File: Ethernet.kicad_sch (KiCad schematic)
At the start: 1 part

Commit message: Wire Ethernet
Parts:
- added R? (x2): 470Ω, symbol Device:R_Small
- added U? (x2): TPD4EUSB30, Package_SON:USON-10_2.5x1.0mm_P0.5mm, symbol Power_Protection:TPD4EUSB30
- gave numbers to parts that had none: 1
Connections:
- net TD1+: now reaches J.1 (TD1+)
- net TD1+: now also U?.1 (D1+)
- net TD4-: now reaches J.10 (TD4-)
- net TD4-: now also U?.5 (D2-)
- net VC1: now reaches J.11 (VC1)
- net VC2: now reaches J.12 (VC2)
- net VC3: now reaches J.13 (VC3)
- net VC4: now reaches J.14 (VC4)
- net +3.3V: now reaches J.15 (LED1+)
- net +3.3V: now also J.17 (LED2+)
- net at J.16 (LED1-): now also R?.2
- net at J.18 (LED2-): now also R?.2
- net TD1-: now reaches J.2 (TD1-)
- net TD1-: now also U?.2 (D1-)
- net TD2+: now reaches J.3 (TD2+)
- net TD2+: now also U?.4 (D2+)
- net TD2-: now reaches J.6 (TD2-)
- net TD2-: now also U?.5 (D2-)
- net TD3+: now reaches J.7 (TD3+)
- net TD3+: now also U?.1 (D1+)
- net TD3-: now reaches J.8 (TD3-)
- net TD3-: now also U?.2 (D1-)
- net TD4+: now reaches J.9 (TD4+)
- net TD4+: now also U?.4 (D2+)
- net GND: now reaches J.SH
- new net: U?.3 (GND), U?.8 (GND) (x2)
- new net LED_GREEN: R?.1
- new net LED_YELLOW: R?.1
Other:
- moved on the sheet: J

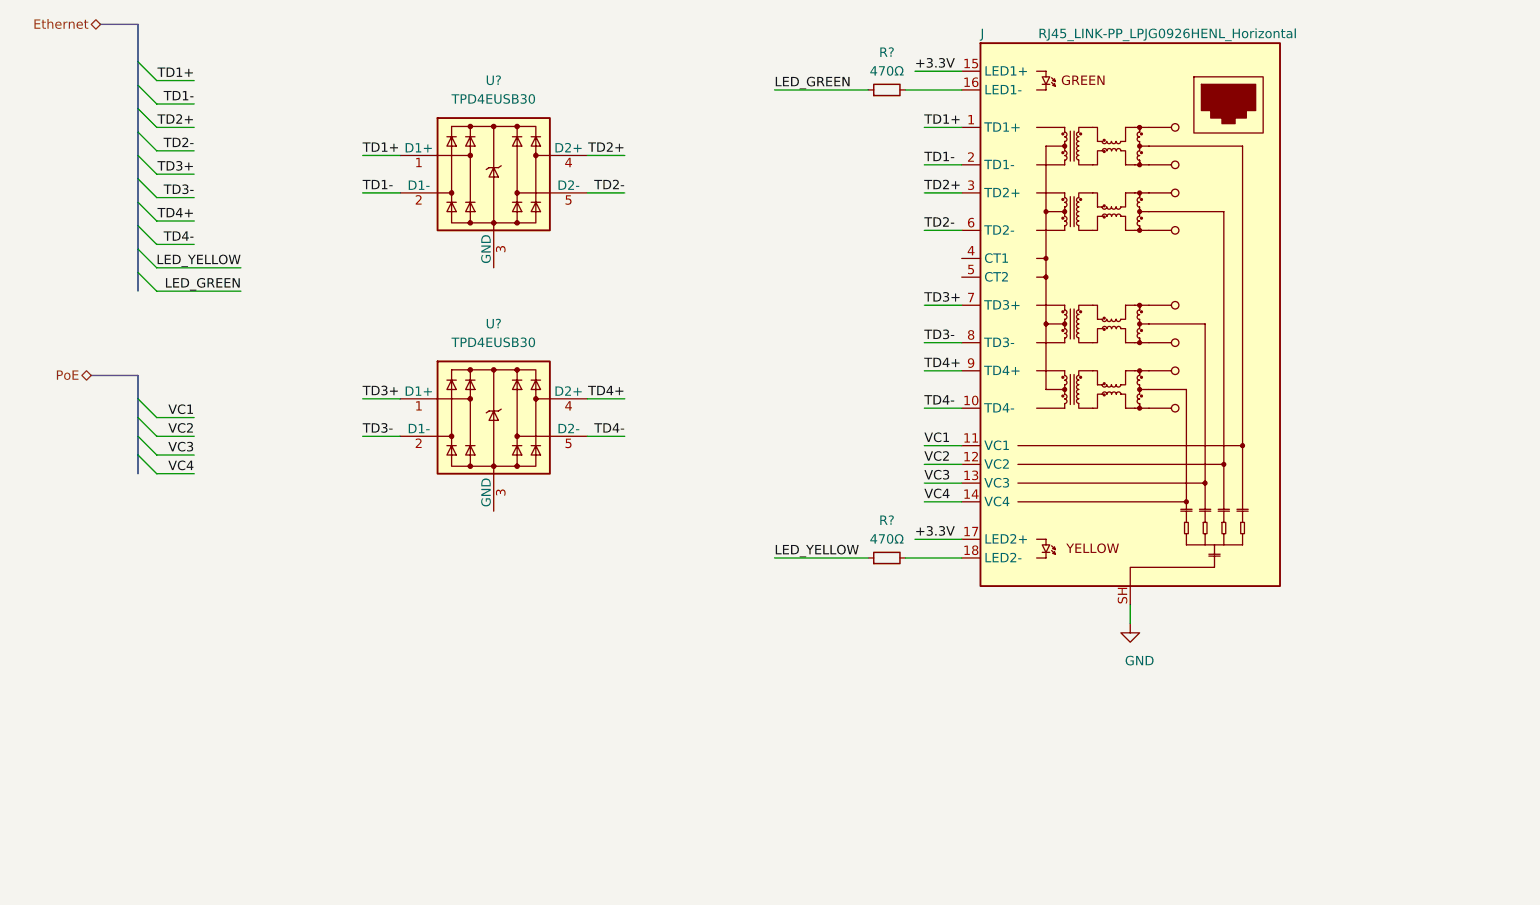
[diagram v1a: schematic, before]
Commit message: Multiple changes in schematic & projects:
    -Added net classes for controlled impedance traces
    -Added power hierarchical sheet
    -Initial USB subsystem schematic
    -Added multiple bus definitions (usb, pcie, i2c etc.)
    -Fixed busses use
    -Added LDO for audio analog rails

Signed-off-by: Dominik Sliwa <dominik@sliwa.io>
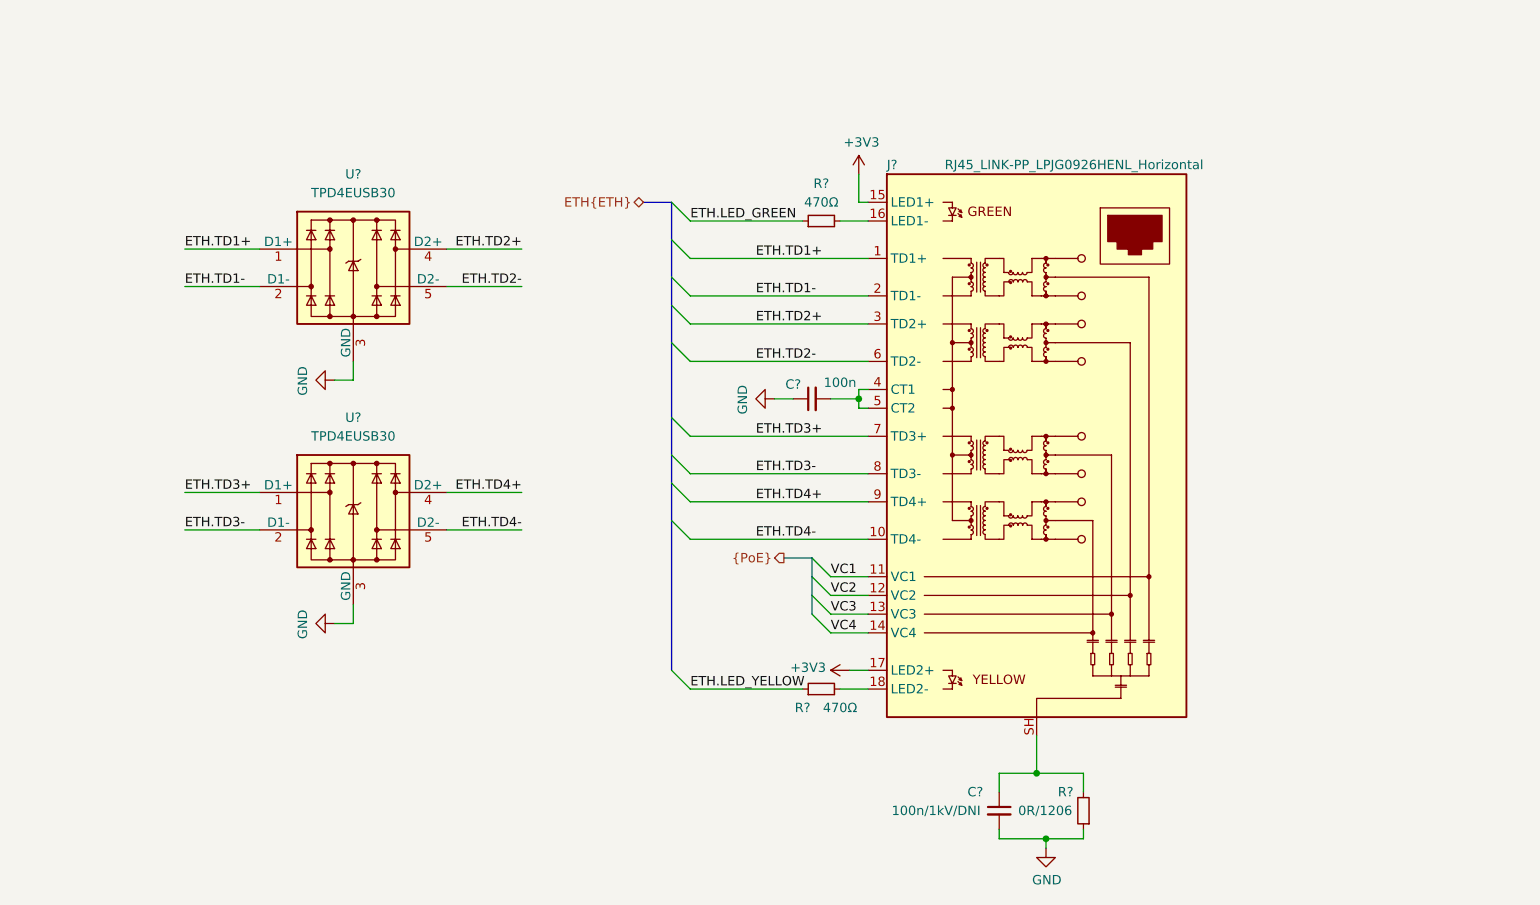
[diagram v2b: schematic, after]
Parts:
- added C?: 100n/1kV/DNI, symbol Device:C_Small
- added C?: 100n, symbol Device:C_Small
- added R?: 0R/1206, symbol Device:R_Small
- renumbered J to J?
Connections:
- net GND: now also U?.3 (GND), U?.3 (GND), U?.8 (GND), U?.8 (GND), C?.1, C?.2, R?.1; no longer J?.SH
- net at J?.4 (CT1): now also J?.5 (CT2), C?.2
- net +3.3V renamed +3V3
- net LED_GREEN renamed ETH.LED_GREEN
- net LED_YELLOW renamed ETH.LED_YELLOW
- net TD1+ renamed ETH.TD1+
- net TD1- renamed ETH.TD1-
- net TD2+ renamed ETH.TD2+
- net TD2- renamed ETH.TD2-
- net TD3+ renamed ETH.TD3+
- net TD3- renamed ETH.TD3-
- net TD4+ renamed ETH.TD4+
- net TD4- renamed ETH.TD4-
- new net: C?.1, J?.SH, R?.2
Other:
- moved on the sheet: J?, R?, U?

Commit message: PoE and clean-up
- Moved PoE to a seperate sheet and finished design
- Started using Config field for Variants and DNP flag
- Fix-ups
- Added Wurth 749119550 and TI TPS23734 to the symbol library
- Changed RTC from PCF8563 to PCF85063

Signed-off-by: Dominik Sliwa <dominik@sliwa.io>
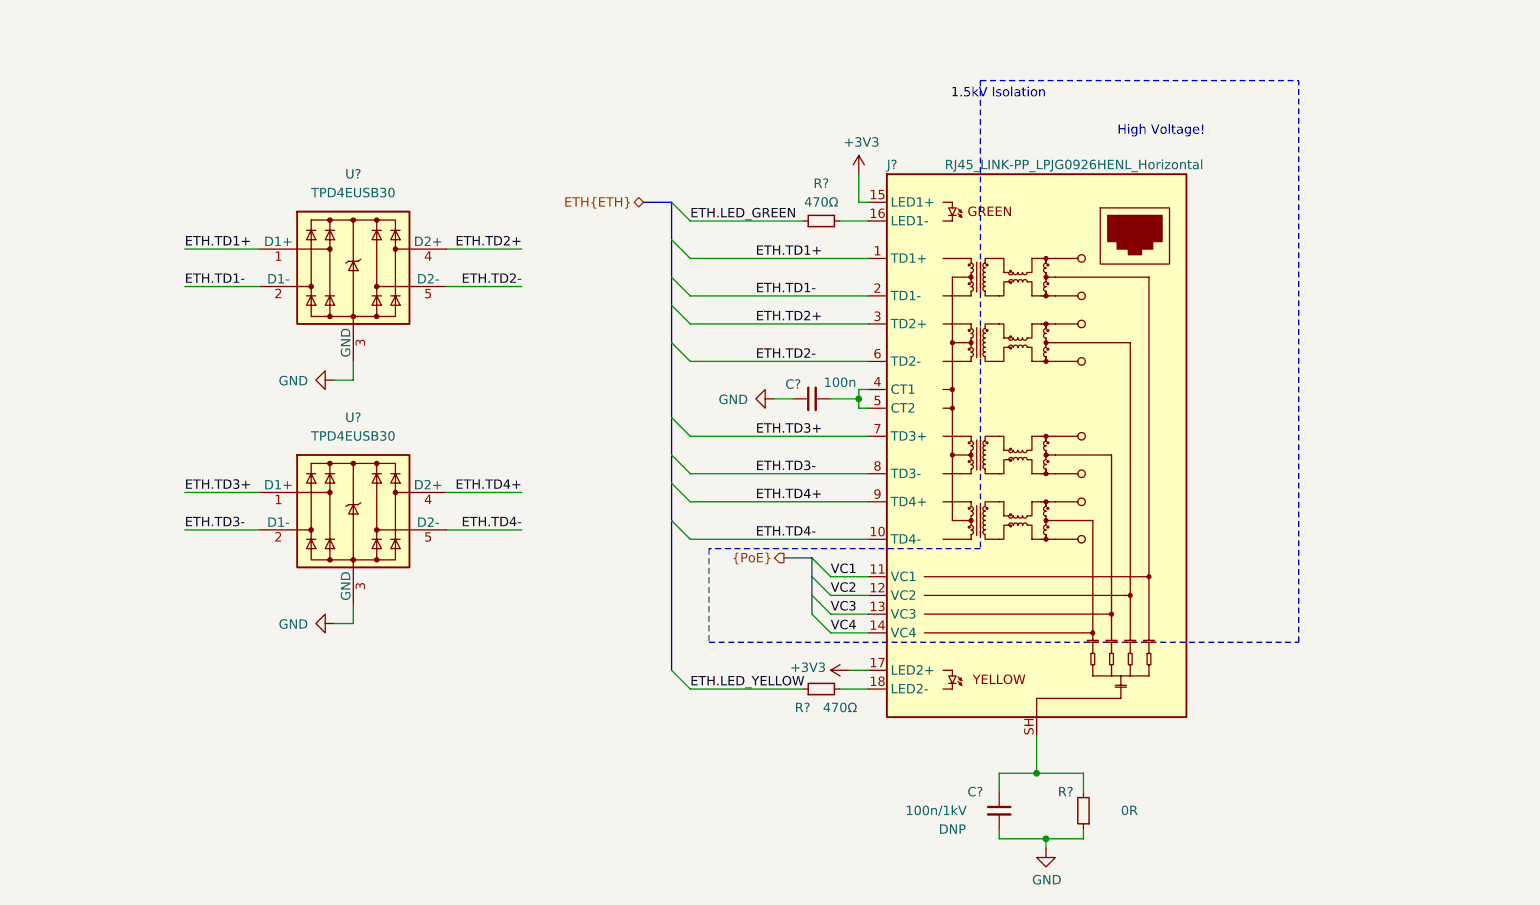
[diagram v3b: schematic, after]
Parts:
- C?: value 100n/1kV/DNI -> 100n/1kV; Config (none) -> DNP
- R?: value 0R/1206 -> 0R
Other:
- note added: "1.5kV Isolation"
- note added: "High Voltage!"
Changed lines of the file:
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@@
     (stroke (width 0) (type solid) (color 0 0 0 0))
+  )
+  (polyline (pts (xy 133.35 100.33) (xy 133.35 113.03))
+    (stroke (width 0) (type dash) (color 0 0 0 0))
+  )
+  (polyline (pts (xy 133.35 113.03) (xy 213.36 113.03))
+    (stroke (width 0) (type dash) (color 0 0 0 0))
+  )
+  (polyline (pts (xy 170.18 36.83) (xy 170.18 100.33))
+    (stroke (width 0) (type dash) (color 0 0 0 0))
+  )
+  (polyline (pts (xy 170.18 36.83) (xy 213.36 36.83))
+    (stroke (width 0) (type dash) (color 0 0 0 0))
+  )
+  (polyline (pts (xy 170.18 100.33) (xy 133.35 100.33))
+    (stroke (width 0) (type dash) (color 0 0 0 0))
+  )
+  (polyline (pts (xy 213.36 113.03) (xy 213.36 36.83))
+    (stroke (width 0) (type dash) (color 0 0 0 0))
+  )
+  (text "1.5kV Isolation" (at 179.07 39.37 180)
+    (effects (font (size 1.27 1.27)) (justify right bottom))
+  )
+  (text "High Voltage!" (at 200.66 44.45 180)
+    (effects (font (size 1.27 1.27)) (justify right bottom))
   )
   (label "ETH.TD1+" (at 62.23 59.69 0)
@@
       (effects (font (size 1.27 1.27)) hide)
     )
-    (property "Value" "GND" (id 1) (at 78.2256 77.5843 0))
+    (property "Value" "GND" (id 1) (at 76.9556 77.5843 90))
     (property "Footprint" "" (id 2) (at 82.55 77.47 0)
       (effects (font (size 1.27 1.27)) hide)
@@
       (effects (font (size 1.27 1.27)) hide)
     )
-    (property "Value" "GND" (id 1) (at 78.2256 110.6043 0))
+    (property "Value" "GND" (id 1) (at 76.9556 110.6043 90))
     (property "Footprint" "" (id 2) (at 82.55 110.49 0)
       (effects (font (size 1.27 1.27)) hide)
@@
       (effects (font (size 1.27 1.27)) hide)
     )
-    (property "Value" "GND" (id 1) (at 137.9156 80.1243 0))
+    (property "Value" "GND" (id 1) (at 136.6456 80.1243 90))
     (property "Footprint" "" (id 2) (at 142.24 80.01 0)
       (effects (font (size 1.27 1.27)) hide)
@@
     (in_bom yes) (on_board yes)
     (property "Reference" "R?" (id 0) (at 181.7432 133.35 0))
-    (property "Value" "0R/1206" (id 1) (at 178.962 135.89 0))
+    (property "Value" "0R" (id 1) (at 190.392 135.89 0))
     (property "Footprint" "" (id 2) (at 184.15 135.89 0)
       (effects (font (size 1.27 1.27)) hide)
@@
     (in_bom yes) (on_board yes)
     (property "Reference" "C?" (id 0) (at 169.4877 133.35 0))
-    (property "Value" "100n/1kV/DNI" (id 1) (at 164.166 135.89 0))
+    (property "Value" "100n/1kV" (id 1) (at 164.166 135.89 0))
     (property "Footprint" "" (id 2) (at 172.72 135.89 0)
       (effects (font (size 1.27 1.27)) hide)
@@
       (effects (font (size 1.27 1.27)) hide)
     )
+    (property "Config" "DNP" (id 4) (at 166.37 138.43 0))
   )
   (symbol (lib_id "Power_Protection:TPD4EUSB30") (at 85.09 62.23 0) (unit 1)

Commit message: Update Manufacturer/PartNumber accross the whole schema
Signed-off-by: Stefan Agner <stefan@agner.ch>
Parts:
- J?: Manufacturer (none) -> LINK-PP; PartNumber (none) -> LPJG0926HENL
- U? (x2): Manufacturer (none) -> Texas Instruments; PartNumber (none) -> TPD4EUSB30DQAR
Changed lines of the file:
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@@
 (kicad_sch (version 20201015) (generator eeschema)
   (paper "A4")
+  (bus_alias "ETH" (members "TD1+" "TD1-" "TD2+" "TD2-" "TD3+" "TD3-" "TD4+" "TD4-" "LED_YELLOW" "LED_GREEN"))
   (bus_alias "PoE" (members "VC1" "VC2" "VC3" "VC4"))
-  (bus_alias "ETH" (members "TD1+" "TD1-" "TD2+" "TD2-" "TD3+" "TD3-" "TD4+" "TD4-" "LED_YELLOW" "LED_GREEN"))
   (junction (at 153.67 80.01) (diameter 0.9144) (color 0 0 0 0))
   (junction (at 177.8 130.81) (diameter 0.9144) (color 0 0 0 0))
@@
   (symbol (lib_id "power:+3V3") (at 152.4 116.84 90) (unit 1)
     (in_bom yes) (on_board yes)
-    (property "Reference" "#PWR?" (id 0) (at 156.21 116.84 0)
+    (property "Reference" "#PWR0182" (id 0) (at 156.21 116.84 0)
       (effects (font (size 1.27 1.27)) hide)
     )
@@
   (symbol (lib_id "power:+3V3") (at 153.67 49.53 0) (unit 1)
     (in_bom yes) (on_board yes)
-    (property "Reference" "#PWR?" (id 0) (at 153.67 53.34 0)
+    (property "Reference" "#PWR0184" (id 0) (at 153.67 53.34 0)
       (effects (font (size 1.27 1.27)) hide)
     )
@@
   (symbol (lib_id "power:GND") (at 82.55 77.47 270) (unit 1)
     (in_bom yes) (on_board yes)
-    (property "Reference" "#PWR?" (id 0) (at 76.2 77.47 0)
+    (property "Reference" "#PWR0181" (id 0) (at 76.2 77.47 0)
       (effects (font (size 1.27 1.27)) hide)
     )
@@
   (symbol (lib_id "power:GND") (at 82.55 110.49 270) (unit 1)
     (in_bom yes) (on_board yes)
-    (property "Reference" "#PWR?" (id 0) (at 76.2 110.49 0)
+    (property "Reference" "#PWR0180" (id 0) (at 76.2 110.49 0)
       (effects (font (size 1.27 1.27)) hide)
     )
@@
   (symbol (lib_id "power:GND") (at 142.24 80.01 270) (unit 1)
     (in_bom yes) (on_board yes)
-    (property "Reference" "#PWR?" (id 0) (at 135.89 80.01 0)
+    (property "Reference" "#PWR0183" (id 0) (at 135.89 80.01 0)
       (effects (font (size 1.27 1.27)) hide)
     )
@@
   (symbol (lib_id "power:GND") (at 179.07 140.97 0) (unit 1)
     (in_bom yes) (on_board yes)
-    (property "Reference" "#PWR?" (id 0) (at 179.07 147.32 0)
+    (property "Reference" "#PWR0179" (id 0) (at 179.07 147.32 0)
       (effects (font (size 1.27 1.27)) hide)
     )
@@
       (effects (font (size 1.27 1.27)) hide)
     )
+    (property "Manufacturer" "Texas Instruments" (id 4) (at 85.09 62.23 0)
+      (effects (font (size 1.27 1.27)) hide)
+    )
+    (property "PartNumber" "TPD4EUSB30DQAR" (id 5) (at 85.09 62.23 0)
+      (effects (font (size 1.27 1.27)) hide)
+    )
   )
   (symbol (lib_id "Power_Protection:TPD4EUSB30") (at 85.09 95.25 0) (unit 1)
@@
       (effects (font (size 1.27 1.27)) hide)
     )
+    (property "Manufacturer" "Texas Instruments" (id 4) (at 85.09 95.25 0)
+      (effects (font (size 1.27 1.27)) hide)
+    )
+    (property "PartNumber" "TPD4EUSB30DQAR" (id 5) (at 85.09 95.25 0)
+      (effects (font (size 1.27 1.27)) hide)
+    )
   )
   (symbol (lib_id "LightBlue:RJ45_LINK-PP_LPJG0926HENL_Horizontal") (at 177.8 86.36 0) (unit 1)
@@
       (effects (font (size 1.27 1.27)) hide)
     )
+    (property "Manufacturer" "LINK-PP" (id 4) (at 177.8 86.36 0)
+      (effects (font (size 1.27 1.27)) hide)
+    )
+    (property "PartNumber" "LPJG0926HENL" (id 5) (at 177.8 86.36 0)
+      (effects (font (size 1.27 1.27)) hide)
+    )

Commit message: Annotate symbools and assign capacitor footprints
Signed-off-by: Stefan Agner <stefan@agner.ch>
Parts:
- C28: renamed from C?; footprint (none) -> Capacitor_SMD:C_0402_1005Metric
- C29: renamed from C?; footprint (none) -> Capacitor_SMD:C_1206_3216Metric
- gave numbers to parts that had none: 6
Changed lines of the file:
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@@
   (symbol (lib_id "Device:R_Small") (at 148.59 55.88 90) (unit 1)
     (in_bom yes) (on_board yes)
-    (property "Reference" "R?" (id 0) (at 148.59 50.8 90))
+    (property "Reference" "R18" (id 0) (at 148.59 50.8 90))
     (property "Value" "470Ω" (id 1) (at 148.59 53.34 90))
     (property "Footprint" "" (id 2) (at 148.59 55.88 0)
@@
   (symbol (lib_id "Device:R_Small") (at 148.59 119.38 90) (unit 1)
     (in_bom yes) (on_board yes)
-    (property "Reference" "R?" (id 0) (at 146.05 121.92 90))
+    (property "Reference" "R19" (id 0) (at 146.05 121.92 90))
     (property "Value" "470Ω" (id 1) (at 151.13 121.92 90))
     (property "Footprint" "" (id 2) (at 148.59 119.38 0)
@@
   (symbol (lib_id "Device:R_Small") (at 184.15 135.89 180) (unit 1)
     (in_bom yes) (on_board yes)
-    (property "Reference" "R?" (id 0) (at 181.7432 133.35 0))
+    (property "Reference" "R20" (id 0) (at 181.7432 133.35 0))
     (property "Value" "0R" (id 1) (at 190.392 135.89 0))
     (property "Footprint" "" (id 2) (at 184.15 135.89 0)
@@
   (symbol (lib_id "Device:C_Small") (at 147.32 80.01 90) (unit 1)
     (in_bom yes) (on_board yes)
-    (property "Reference" "C?" (id 0) (at 144.78 78.0477 90))
+    (property "Reference" "C28" (id 0) (at 144.78 78.0477 90))
     (property "Value" "100n" (id 1) (at 151.13 77.806 90))
-    (property "Footprint" "" (id 2) (at 147.32 80.01 0)
+    (property "Footprint" "Capacitor_SMD:C_0402_1005Metric" (id 2) (at 147.32 80.01 0)
       (effects (font (size 1.27 1.27)) hide)
     )
@@
   (symbol (lib_id "Device:C_Small") (at 172.72 135.89 0) (unit 1)
     (in_bom yes) (on_board yes)
-    (property "Reference" "C?" (id 0) (at 169.4877 133.35 0))
+    (property "Reference" "C29" (id 0) (at 169.4877 133.35 0))
     (property "Value" "100n/1kV" (id 1) (at 164.166 135.89 0))
-    (property "Footprint" "" (id 2) (at 172.72 135.89 0)
+    (property "Footprint" "Capacitor_SMD:C_1206_3216Metric" (id 2) (at 172.72 135.89 0)
       (effects (font (size 1.27 1.27)) hide)
     )
@@
   (symbol (lib_id "Power_Protection:TPD4EUSB30") (at 85.09 62.23 0) (unit 1)
     (in_bom yes) (on_board yes)
-    (property "Reference" "U?" (id 0) (at 85.09 49.53 0))
+    (property "Reference" "U12" (id 0) (at 85.09 49.53 0))
     (property "Value" "TPD4EUSB30" (id 1) (at 85.09 52.07 0))
     (property "Footprint" "Package_SON:USON-10_2.5x1.0mm_P0.5mm" (id 2) (at 60.96 72.39 0)
@@
   (symbol (lib_id "Power_Protection:TPD4EUSB30") (at 85.09 95.25 0) (unit 1)
     (in_bom yes) (on_board yes)
-    (property "Reference" "U?" (id 0) (at 85.09 82.55 0))
+    (property "Reference" "U13" (id 0) (at 85.09 82.55 0))
     (property "Value" "TPD4EUSB30" (id 1) (at 85.09 85.09 0))
     (property "Footprint" "Package_SON:USON-10_2.5x1.0mm_P0.5mm" (id 2) (at 60.96 105.41 0)
@@
   (symbol (lib_id "LightBlue:RJ45_LINK-PP_LPJG0926HENL_Horizontal") (at 177.8 86.36 0) (unit 1)
     (in_bom yes) (on_board yes)
-    (property "Reference" "J?" (id 0) (at 157.48 48.26 0)
+    (property "Reference" "J9" (id 0) (at 157.48 48.26 0)
       (effects (font (size 1.27 1.27)) (justify left))
     )

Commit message: Standardize page settings/add page titles
Signed-off-by: Stefan Agner <stefan@agner.ch>
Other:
- company: (none) -> Nabu Casa
- title: (none) -> Ethernet
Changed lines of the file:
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@@
 (kicad_sch (version 20201015) (generator eeschema)
   (paper "A4")
+  (title_block
+    (title "Ethernet")
+    (date "2021-01-12")
+    (rev "0.1")
+    (company "Nabu Casa")
+    (comment 1 "www.nabucasa.com")
+    (comment 2 "Light Blue")
+  )
   (bus_alias "ETH" (members "TD1+" "TD1-" "TD2+" "TD2-" "TD3+" "TD3-" "TD4+" "TD4-" "LED_YELLOW" "LED_GREEN"))
   (bus_alias "PoE" (members "VC1" "VC2" "VC3" "VC4"))
